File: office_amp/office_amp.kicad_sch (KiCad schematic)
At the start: 0 parts

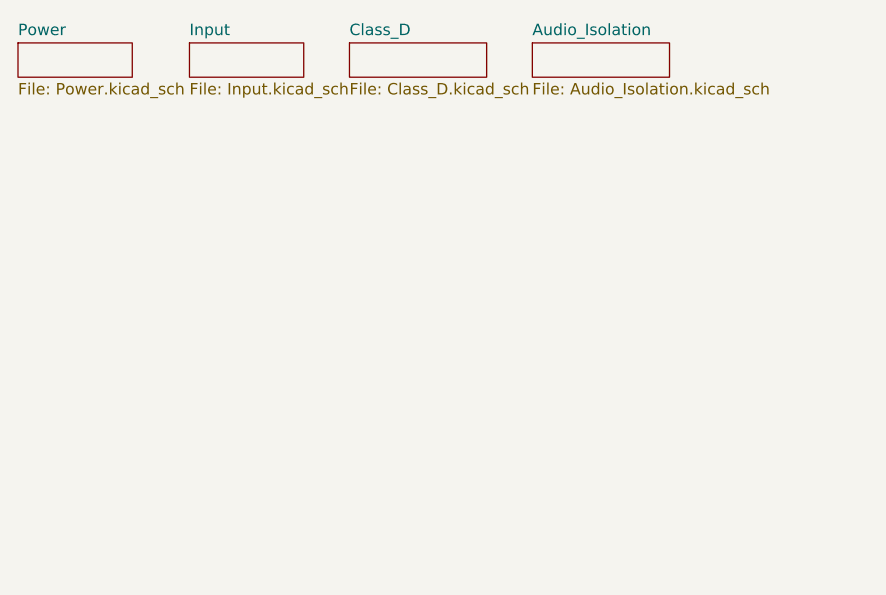
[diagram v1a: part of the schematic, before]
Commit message: First positioning of new components (top site), added mounting holes for case  compabillity (Donau 523178)
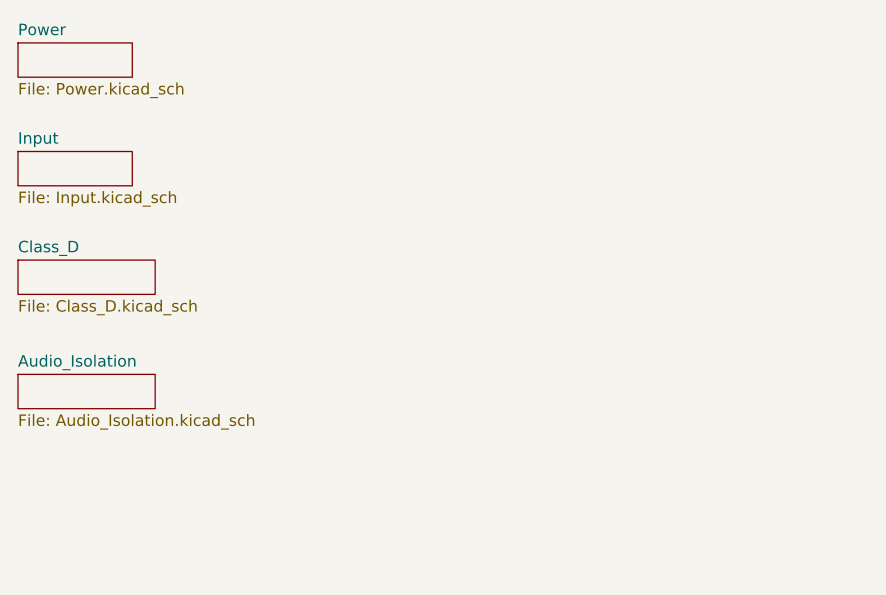
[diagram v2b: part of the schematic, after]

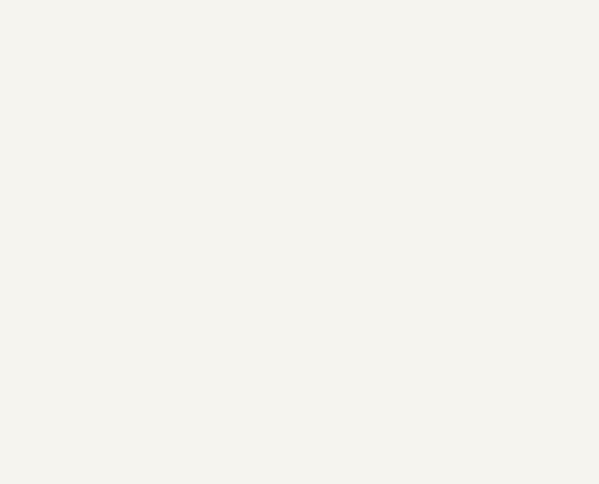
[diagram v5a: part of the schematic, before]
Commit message: First layout touch interface
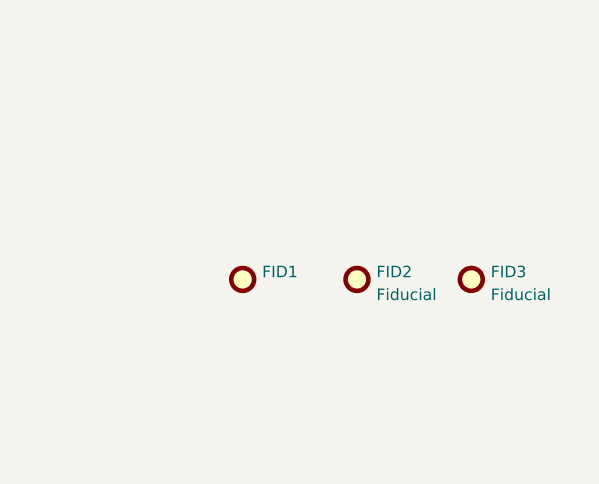
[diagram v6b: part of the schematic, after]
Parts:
- added FID1: (no value), symbol Mechanical:Fiducial
- added FID2, FID3: Fiducial, Fiducial:Fiducial_1.5mm_Mask3mm, symbol Mechanical:Fiducial
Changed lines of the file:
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@@
     (effects (font (size 1.27 1.27)) (justify left bottom))
+  )
+  (symbol (lib_id "Mechanical:Fiducial") (at 177.8 161.29 0) (unit 1)
+    (in_bom yes) (on_board yes) (fields_autoplaced)
+    (property "Reference" "FID1" (id 0) (at 179.959 160.4553 0)
+      (effects (font (size 1.27 1.27)) (justify left))
+    )
+    (property "Value" "" (id 1) (at 179.959 162.9922 0)
+      (effects (font (size 1.27 1.27)) (justify left))
+    )
+    (property "Footprint" "" (id 2) (at 177.8 161.29 0)
+      (effects (font (size 1.27 1.27)) hide)
+    )
+    (property "Datasheet" "~" (id 3) (at 177.8 161.29 0)
+      (effects (font (size 1.27 1.27)) hide)
+    )
+  )
+  (symbol (lib_id "Mechanical:Fiducial") (at 190.5 161.29 0) (unit 1)
+    (in_bom yes) (on_board yes) (fields_autoplaced)
+    (property "Reference" "FID2" (id 0) (at 192.659 160.4553 0)
+      (effects (font (size 1.27 1.27)) (justify left))
+    )
+    (property "Value" "Fiducial" (id 1) (at 192.659 162.9922 0)
+      (effects (font (size 1.27 1.27)) (justify left))
+    )
+    (property "Footprint" "Fiducial:Fiducial_1.5mm_Mask3mm" (id 2) (at 190.5 161.29 0)
+      (effects (font (size 1.27 1.27)) hide)
+    )
+    (property "Datasheet" "~" (id 3) (at 190.5 161.29 0)
+      (effects (font (size 1.27 1.27)) hide)
+    )
+  )
+  (symbol (lib_id "Mechanical:Fiducial") (at 203.2 161.29 0) (unit 1)
+    (in_bom yes) (on_board yes) (fields_autoplaced)
+    (property "Reference" "FID3" (id 0) (at 205.359 160.4553 0)
+      (effects (font (size 1.27 1.27)) (justify left))
+    )
+    (property "Value" "Fiducial" (id 1) (at 205.359 162.9922 0)
+      (effects (font (size 1.27 1.27)) (justify left))
+    )
+    (property "Footprint" "Fiducial:Fiducial_1.5mm_Mask3mm" (id 2) (at 203.2 161.29 0)
+      (effects (font (size 1.27 1.27)) hide)
+    )
+    (property "Datasheet" "~" (id 3) (at 203.2 161.29 0)
+      (effects (font (size 1.27 1.27)) hide)
+    )
   )
   (sheet (at 16.51 17.78) (size 12.7 3.81) (fields_autoplaced)
@@
       (reference "D6") (unit 1) (value "1N4148W") (footprint "Diode_SMD:D_SOD-123")
     )
+    (path "/6887f346-34fb-47be-9aca-e3608346da89"
+      (reference "FID1") (unit 1) (value "Fiducial") (footprint "Fiducial:Fiducial_1.5mm_Mask3mm")
+    )
+    (path "/9cf05b35-668e-4e1c-971f-999d17f0efd5"
+      (reference "FID2") (unit 1) (value "Fiducial") (footprint "Fiducial:Fiducial_1.5mm_Mask3mm")
+    )
+    (path "/e6fdf062-8946-4c6b-8a4e-0713bfd356f1"
+      (reference "FID3") (unit 1) (value "Fiducial") (footprint "Fiducial:Fiducial_1.5mm_Mask3mm")
+    )
     (path "/00000000-0000-0000-0000-00005ec853eb/00000000-0000-0000-0000-00005ed17c8e"
       (reference "J1") (unit 1) (value "Jack-DC") (footprint "Connector_BarrelJack:BarrelJack_Horizontal")
@@
     )
     (path "/00000000-0000-0000-0000-00005ec853eb/00000000-0000-0000-0000-0000608e6d0f"
-      (reference "U2") (unit 1) (value "TBA_2-2421") (footprint "MyLib:SIP-7")
+      (reference "U2") (unit 1) (value "TBA_2-2421") (footprint "office_amp:SIP-7")
     )
     (path "/00000000-0000-0000-0000-000060794134/e1080cb7-b3b4-4124-998e-e35028b100b2"
@@
     )
     (path "/00000000-0000-0000-0000-00005ec853eb/00000000-0000-0000-0000-00005f835065"
-      (reference "U4") (unit 1) (value "TBA_2-2421") (footprint "MyLib:SIP-7")
+      (reference "U4") (unit 1) (value "TBA_2-2421") (footprint "office_amp:SIP-7")
     )
     (path "/00000000-0000-0000-0000-00005ed110e5/00000000-0000-0000-0000-00005fc6fbee"

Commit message: Changes from testing
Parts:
- FID1: value (none) -> Fiducial; footprint (none) -> Fiducial:Fiducial_1.5mm_Mask3mm
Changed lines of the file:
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@@
       (effects (font (size 1.27 1.27)) (justify left))
     )
-    (property "Value" "" (id 1) (at 179.959 162.9922 0)
+    (property "Value" "Fiducial" (id 1) (at 179.959 162.9922 0)
       (effects (font (size 1.27 1.27)) (justify left))
     )
-    (property "Footprint" "" (id 2) (at 177.8 161.29 0)
+    (property "Footprint" "Fiducial:Fiducial_1.5mm_Mask3mm" (id 2) (at 177.8 161.29 0)
       (effects (font (size 1.27 1.27)) hide)
     )
